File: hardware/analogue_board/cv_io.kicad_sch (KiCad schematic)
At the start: 75 parts, among them J410 Holes, left top, J411 Holes, left bottom, J412 Holes, right top, J413 Holes, right top, J414 Holes, right middle, J415 Holes, right middle, U401 ADS8688IDBTR, U402 DG412DQ-T1-E3, U403 DG412DQ-T1-E3

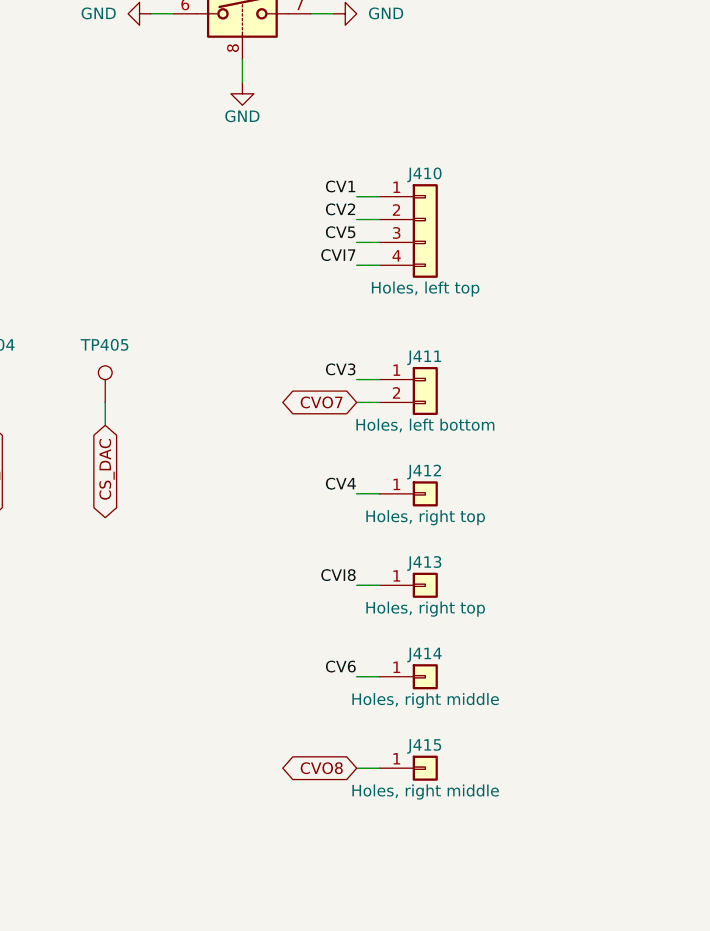
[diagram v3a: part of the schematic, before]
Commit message: Analogue board: bus chips level with their module pins; design rules; trial autoroute
Re-floorplan the centre channel in the order of the module's buses (SPI-A,
SPI-B, I2S, I2C), so the codec is 6 mm from the Pico's I2S pins instead of
38 mm; CV output op-amps move to the top-right corner.

Net classes (0.15/0.15 default, 0.3 power) and an In1 ground plane are
written into the project. autoroute.py runs Freerouting on a copy of the
board to measure routability. Schematic hole groups no longer overlap.

Co-Authored-By: Claude Opus 5.5 <noreply@anthropic.com>
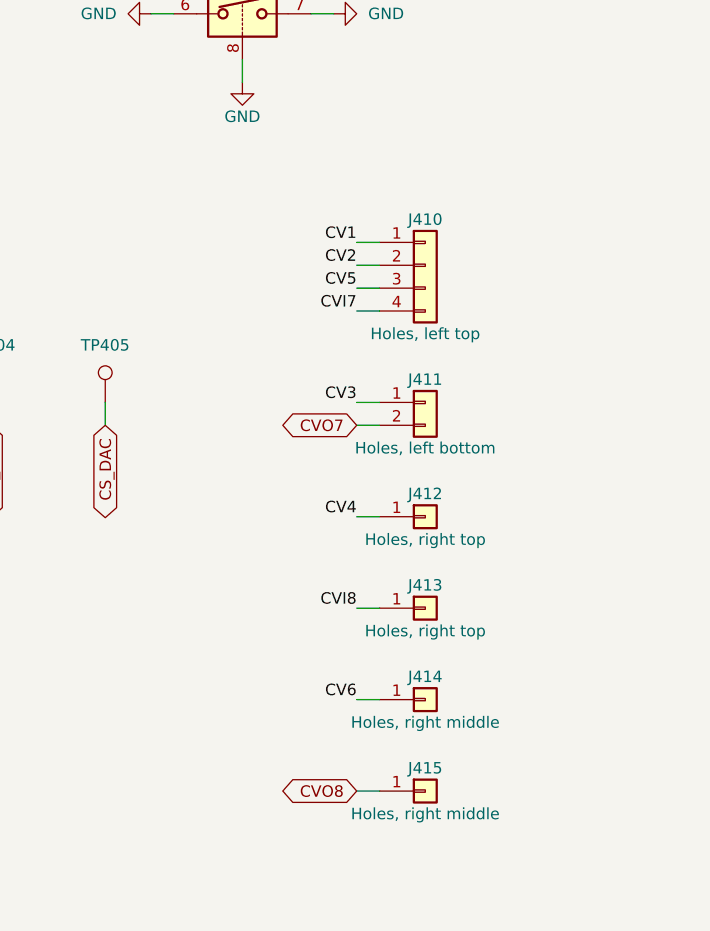
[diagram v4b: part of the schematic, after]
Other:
- moved on the sheet: J410, J411, J412, J413, J414, J415
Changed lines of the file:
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@@
 	(symbol
 		(lib_id "Connector_Generic:Conn_01x04")
-		(at 350.52 139.7 0)
+		(at 350.52 144.78 0)
 		(unit 1)
 		(exclude_from_sim no)
@@
 		(dnp no)
 		(property "Reference" "J410"
-			(at 350.52 134.62 0)
+			(at 350.52 139.7 0)
 			(effects
 				(font (size 1.27 1.27))
@@
 		)
 		(property "Value" "Holes, left top"
-			(at 350.52 147.32 0)
+			(at 350.52 152.4 0)
 			(effects
 				(font (size 1.27 1.27))
@@
 		)
 		(property "Footprint" "analogue_board:WiringHoles_1x04"
-			(at 350.52 139.7 0)
+			(at 350.52 144.78 0)
 			(effects
 				(font (size 1.27 1.27))
@@
 		)
 		(property "Datasheet" ""
-			(at 350.52 139.7 0)
+			(at 350.52 144.78 0)
 			(effects
 				(font (size 1.27 1.27))
@@
 		)
 		(property "Description" ""
-			(at 350.52 139.7 0)
+			(at 350.52 144.78 0)
 			(effects
 				(font (size 1.27 1.27))
@@
 		)
 		(property "JLC" "bare holes"
-			(at 350.52 139.7 0)
+			(at 350.52 144.78 0)
 			(effects
 				(font (size 1.27 1.27))
@@
 	)
 	(label "CV1"
-		(at 342.9 137.16 180)
+		(at 342.9 142.24 180)
 		(effects
 			(font (size 1.27 1.27))
@@
 	)
 	(label "CV2"
-		(at 342.9 139.7 180)
+		(at 342.9 144.78 180)
 		(effects
 			(font (size 1.27 1.27))
@@
 	)
 	(label "CV5"
-		(at 342.9 142.24 180)
+		(at 342.9 147.32 180)
 		(effects
 			(font (size 1.27 1.27))
@@
 	)
 	(label "CVI7"
-		(at 342.9 144.78 180)
+		(at 342.9 149.86 180)
 		(effects
 			(font (size 1.27 1.27))
@@
 	(symbol
 		(lib_id "Connector_Generic:Conn_01x02")
-		(at 350.52 157.48 0)
+		(at 350.52 160.02 0)
 		(unit 1)
 		(exclude_from_sim no)
@@
 		(dnp no)
 		(property "Reference" "J411"
-			(at 350.52 154.94 0)
+			(at 350.52 157.48 0)
 			(effects
 				(font (size 1.27 1.27))
@@
 		)
 		(property "Value" "Holes, left bottom"
-			(at 350.52 162.56 0)
+			(at 350.52 165.1 0)
 			(effects
 				(font (size 1.27 1.27))
@@
 		)
 		(property "Footprint" "analogue_board:WiringHoles_1x02"
-			(at 350.52 157.48 0)
+			(at 350.52 160.02 0)
 			(effects
 				(font (size 1.27 1.27))
@@
 		)
 		(property "Datasheet" ""
-			(at 350.52 157.48 0)
+			(at 350.52 160.02 0)
 			(effects
 				(font (size 1.27 1.27))
@@
 		)
 		(property "Description" ""
-			(at 350.52 157.48 0)
+			(at 350.52 160.02 0)
 			(effects
 				(font (size 1.27 1.27))
@@
 		)
 		(property "JLC" "bare holes"
-			(at 350.52 157.48 0)
+			(at 350.52 160.02 0)
 			(effects
 				(font (size 1.27 1.27))
@@
 	)
 	(label "CV3"
-		(at 342.9 157.48 180)
+		(at 342.9 160.02 180)
 		(effects
 			(font (size 1.27 1.27))
@@
 	(global_label "CVO7"
 		(shape bidirectional)
-		(at 342.9 160.02 180)
+		(at 342.9 162.56 180)
 		(fields_autoplaced yes)
 		(effects
@@
 		)
 		(property "Intersheetrefs" "${INTERSHEET_REFS}"
-			(at 342.9 160.02 0)
+			(at 342.9 162.56 0)
 			(effects
 				(font (size 1.27 1.27))
@@
 	(symbol
 		(lib_id "Connector_Generic:Conn_01x01")
-		(at 350.52 170.18 0)
+		(at 350.52 172.72 0)
 		(unit 1)
 		(exclude_from_sim no)
@@
 		(dnp no)
 		(property "Reference" "J412"
-			(at 350.52 167.64 0)
+			(at 350.52 170.18 0)
 			(effects
 				(font (size 1.27 1.27))
@@
 		)
 		(property "Value" "Holes, right top"
+			(at 350.52 175.26 0)
+			(effects
+				(font (size 1.27 1.27))
+			)
+		)
+		(property "Footprint" "analogue_board:WiringHoles_1x01"
 			(at 350.52 172.72 0)
 			(effects
 				(font (size 1.27 1.27))
-			)
-		)
-		(property "Footprint" "analogue_board:WiringHoles_1x01"
-			(at 350.52 170.18 0)
-			(effects
-				(font (size 1.27 1.27))
 				(hide yes)
 			)
 		)
 		(property "Datasheet" ""
-			(at 350.52 170.18 0)
+			(at 350.52 172.72 0)
 			(effects
 				(font (size 1.27 1.27))
@@
 		)
 		(property "Description" ""
-			(at 350.52 170.18 0)
+			(at 350.52 172.72 0)
 			(effects
 				(font (size 1.27 1.27))
@@
 		)
 		(property "JLC" "bare holes"
-			(at 350.52 170.18 0)
+			(at 350.52 172.72 0)
 			(effects
 				(font (size 1.27 1.27))
@@
 	)
 	(label "CV4"
-		(at 342.9 170.18 180)
+		(at 342.9 172.72 180)
 		(effects
 			(font (size 1.27 1.27))
@@
 	(symbol
 		(lib_id "Connector_Generic:Conn_01x01")
-		(at 350.52 180.34 0)
+		(at 350.52 182.88 0)
 		(unit 1)
 		(exclude_from_sim no)
@@
 		(dnp no)
 		(property "Reference" "J413"
-			(at 350.52 177.8 0)
+			(at 350.52 180.34 0)
 			(effects
 				(font (size 1.27 1.27))
@@
 		)
 		(property "Value" "Holes, right top"
+			(at 350.52 185.42 0)
+			(effects
+				(font (size 1.27 1.27))
+			)
+		)
+		(property "Footprint" "analogue_board:WiringHoles_1x01"
 			(at 350.52 182.88 0)
 			(effects
 				(font (size 1.27 1.27))
-			)
-		)
-		(property "Footprint" "analogue_board:WiringHoles_1x01"
-			(at 350.52 180.34 0)
-			(effects
-				(font (size 1.27 1.27))
 				(hide yes)
 			)
 		)
 		(property "Datasheet" ""
-			(at 350.52 180.34 0)
+			(at 350.52 182.88 0)
 			(effects
 				(font (size 1.27 1.27))
@@
 		)
 		(property "Description" ""
-			(at 350.52 180.34 0)
+			(at 350.52 182.88 0)
 			(effects
 				(font (size 1.27 1.27))
@@
 		)
 		(property "JLC" "bare holes"
-			(at 350.52 180.34 0)
+			(at 350.52 182.88 0)
 			(effects
 				(font (size 1.27 1.27))
@@
 	)
 	(label "CVI8"
-		(at 342.9 180.34 180)
+		(at 342.9 182.88 180)
 		(effects
 			(font (size 1.27 1.27))
@@
 	(symbol
 		(lib_id "Connector_Generic:Conn_01x01")
-		(at 350.52 190.5 0)
+		(at 350.52 193.04 0)
 		(unit 1)
 		(exclude_from_sim no)
@@
 		(dnp no)
 		(property "Reference" "J414"
-			(at 350.52 187.96 0)
+			(at 350.52 190.5 0)
 			(effects
 				(font (size 1.27 1.27))
@@
 		)
 		(property "Value" "Holes, right middle"
+			(at 350.52 195.58 0)
+			(effects
+				(font (size 1.27 1.27))
+			)
+		)
+		(property "Footprint" "analogue_board:WiringHoles_1x01"
 			(at 350.52 193.04 0)
 			(effects
 				(font (size 1.27 1.27))
-			)
-		)
-		(property "Footprint" "analogue_board:WiringHoles_1x01"
-			(at 350.52 190.5 0)
-			(effects
-				(font (size 1.27 1.27))
 				(hide yes)
 			)
 		)
 		(property "Datasheet" ""
-			(at 350.52 190.5 0)
+			(at 350.52 193.04 0)
 			(effects
 				(font (size 1.27 1.27))
@@
 		)
 		(property "Description" ""
-			(at 350.52 190.5 0)
+			(at 350.52 193.04 0)
 			(effects
 				(font (size 1.27 1.27))
@@
 		)
 		(property "JLC" "bare holes"
-			(at 350.52 190.5 0)
+			(at 350.52 193.04 0)
 			(effects
 				(font (size 1.27 1.27))
@@
 	)
 	(label "CV6"
-		(at 342.9 190.5 180)
+		(at 342.9 193.04 180)
 		(effects
 			(font (size 1.27 1.27))
@@
 	(symbol
 		(lib_id "Connector_Generic:Conn_01x01")
-		(at 350.52 200.66 0)
+		(at 350.52 203.2 0)
 		(unit 1)
 		(exclude_from_sim no)
@@
 		(dnp no)
 		(property "Reference" "J415"
-			(at 350.52 198.12 0)
+			(at 350.52 200.66 0)
 			(effects
 				(font (size 1.27 1.27))
@@
 		)
 		(property "Value" "Holes, right middle"
+			(at 350.52 205.74 0)
+			(effects
+				(font (size 1.27 1.27))
+			)
+		)
+		(property "Footprint" "analogue_board:WiringHoles_1x01"
 			(at 350.52 203.2 0)
 			(effects
 				(font (size 1.27 1.27))
-			)
-		)
-		(property "Footprint" "analogue_board:WiringHoles_1x01"
-			(at 350.52 200.66 0)
-			(effects
-				(font (size 1.27 1.27))
 				(hide yes)
 			)
 		)
 		(property "Datasheet" ""
-			(at 350.52 200.66 0)
+			(at 350.52 203.2 0)
 			(effects
 				(font (size 1.27 1.27))
@@
 		)
 		(property "Description" ""
-			(at 350.52 200.66 0)
+			(at 350.52 203.2 0)
 			(effects
 				(font (size 1.27 1.27))
@@
 		)
 		(property "JLC" "bare holes"
-			(at 350.52 200.66 0)
+			(at 350.52 203.2 0)
 			(effects
 				(font (size 1.27 1.27))
@@
 	(global_label "CVO8"
 		(shape bidirectional)
-		(at 342.9 200.66 180)
+		(at 342.9 203.2 180)
 		(fields_autoplaced yes)
 		(effects
@@
 		)
 		(property "Intersheetrefs" "${INTERSHEET_REFS}"
-			(at 342.9 200.66 0)
+			(at 342.9 203.2 0)
 			(effects
 				(font (size 1.27 1.27))
@@
 	)
 	(wire
-		(pts (xy 342.9 137.16) (xy 345.44 137.16))
-		(stroke (width 0) (type default))
-	)
-	(wire
-		(pts (xy 342.9 139.7) (xy 345.44 139.7))
-		(stroke (width 0) (type default))
-	)
-	(wire
 		(pts (xy 342.9 142.24) (xy 345.44 142.24))
 		(stroke (width 0) (type default))
@@
 	)
 	(wire
-		(pts (xy 342.9 157.48) (xy 345.44 157.48))
+		(pts (xy 342.9 147.32) (xy 345.44 147.32))
+		(stroke (width 0) (type default))
+	)
+	(wire
+		(pts (xy 342.9 149.86) (xy 345.44 149.86))
 		(stroke (width 0) (type default))
 	)
@@
 	)
 	(wire
-		(pts (xy 342.9 170.18) (xy 345.44 170.18))
-		(stroke (width 0) (type default))
-	)
-	(wire
-		(pts (xy 342.9 180.34) (xy 345.44 180.34))
-		(stroke (width 0) (type default))
-	)
-	(wire
-		(pts (xy 342.9 190.5) (xy 345.44 190.5))
-		(stroke (width 0) (type default))
-	)
-	(wire
-		(pts (xy 342.9 200.66) (xy 345.44 200.66))
-		(stroke (width 0) (type default))
-	)
+		(pts (xy 342.9 162.56) (xy 345.44 162.56))
+		(stroke (width 0) (type default))
+	)
+	(wire
+		(pts (xy 342.9 172.72) (xy 345.44 172.72))
+		(stroke (width 0) (type default))
+	)
+	(wire
+		(pts (xy 342.9 182.88) (xy 345.44 182.88))
+		(stroke (width 0) (type default))
+	)
+	(wire
+		(pts (xy 342.9 193.04) (xy 345.44 193.04))
+		(stroke (width 0) (type default))
+	)
+	(wire
+		(pts (xy 342.9 203.2) (xy 345.44 203.2))
+		(stroke (width 0) (type default))
+	)
